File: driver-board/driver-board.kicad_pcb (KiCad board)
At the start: 2 copper layers, 105.1 x 41 mm, 78 parts, among them J1 Conn_01x02, J11 Conn_01x04, J2 Conn_01x02, J3 Conn_01x02, J4 Conn_01x02, J5 Conn_01x02, J6 Conn_01x02, J7 Conn_01x02, J8 Conn_01x02, J9 Conn_01x06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

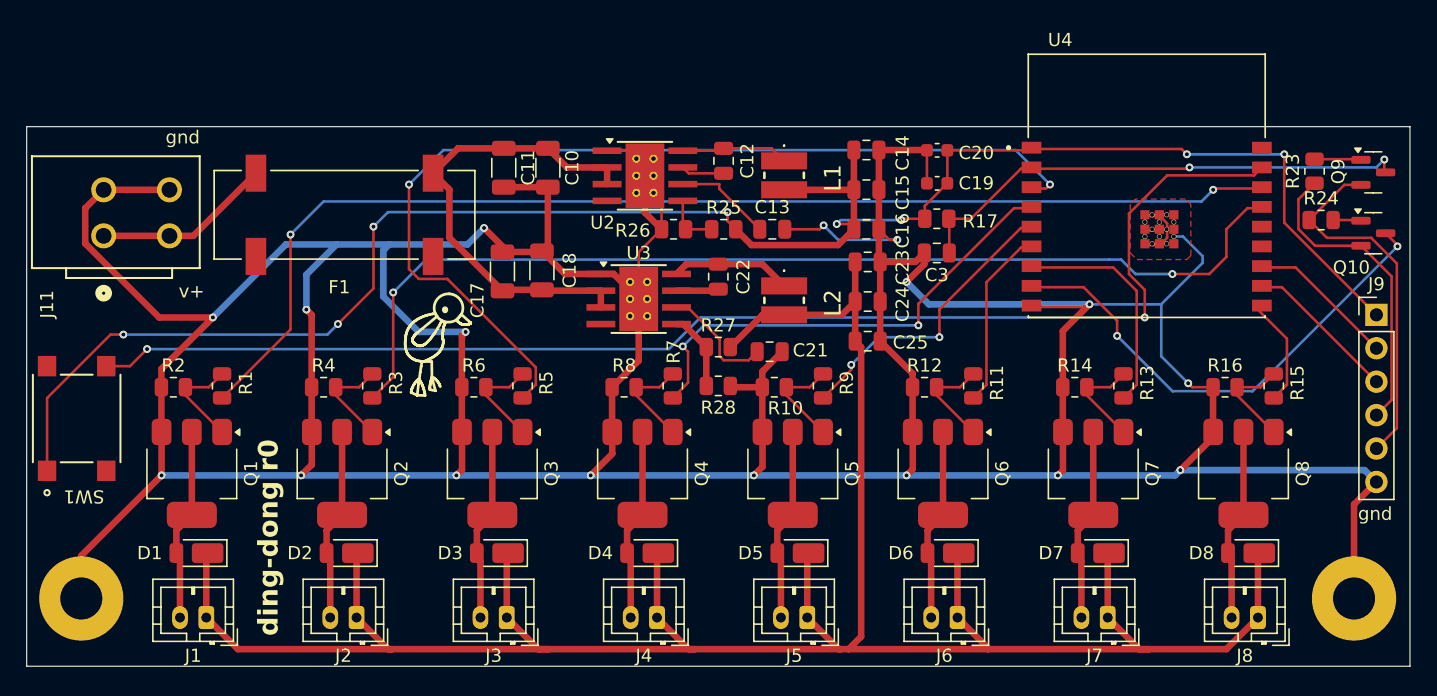
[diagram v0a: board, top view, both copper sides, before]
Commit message: updated layout
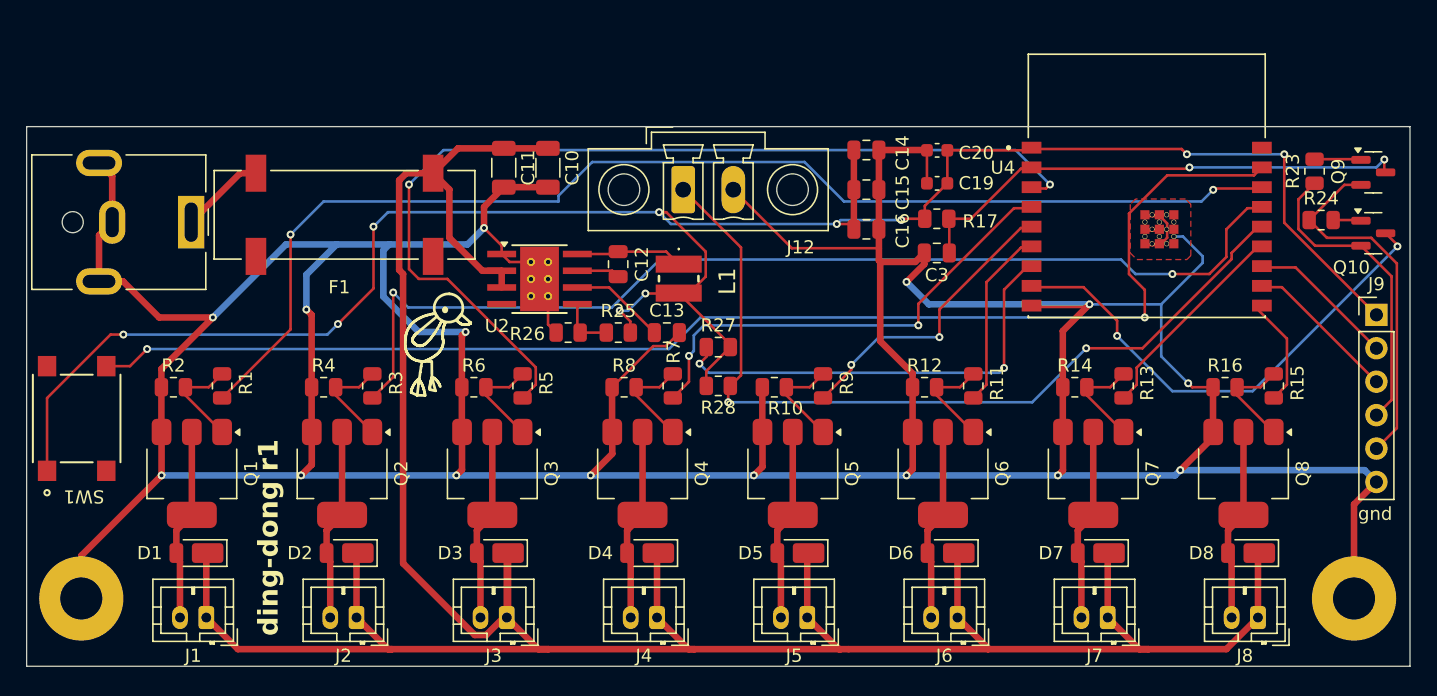
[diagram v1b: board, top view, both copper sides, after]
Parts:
- removed C17: 10uF 50V, Capacitor_SMD:C_1206_3216Metric
- removed C18: .022uF 50V, Capacitor_SMD:C_1206_3216Metric
- removed C21: 1uF, Capacitor_SMD:C_0805_2012Metric
- removed C22: 0.1uF, Capacitor_SMD:C_0805_2012Metric
- removed C23, C24, C25: 10uF, Capacitor_SMD:C_0805_2012Metric
- removed J11: Conn_01x04, footprints:CONN2_2601-3102_WAG
- removed L2: 47uH, footprints:SRN3010C2R2M
- removed U3: LMR36510ADDA, Package_SO:Texas_HTSOP-8-1EP_3.9x4.9mm_P1.27mm_EP2.95x4.9mm_Mask2.4x3.1mm_ThermalVias
- added J10: PJ-063AH, Connector_BarrelJack:BarrelJack_CUI_PJ-063AH_Horizontal, F.Cu at (75.8, 88.8)
- added J12: Conn_01x02, Connector_Phoenix_MC:PhoenixContact_MCV_1,5_2-GF-3.81_1x02_P3.81mm_Vertical_ThreadedFlange_MountHole, F.Cu at (113.1, 86.3)
- R27: value 100k -> 10k
- R28: value 9.09k -> 10k
- moved C12 11.2 mm to (108.2, 92.0)
- moved C13 11.2 mm to (111.9, 97.2)
- moved R25 11.2 mm to (108.2, 97.2)
- moved R26 11.2 mm to (104.4, 97.2)
- moved L1 11.2 mm to (112.8, 93.0)
- moved U2 11.2 mm to (102.2, 93.1)
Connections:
- C10 pad 1: /power/V_FUSED -> +12V
- C11 pad 1: /power/V_FUSED -> +12V
- F1 pad 2_1: /power/V_FUSED -> +12V
- R27 pad 1: Net-(U3-FB) -> Net-(U4-IO8)
- R27 pad 2: +12V -> +3.3V
- R28 pad 1: GND -> Net-(J12-Pin_1)
- R28 pad 2: Net-(U3-FB) -> +3.3V
- U2 pad 2: /power/V_FUSED -> +12V
- U2 pad 3: /power/V_FUSED -> +12V
- U4 pad 13: unconnected-(U4-IO18-Pad13) -> /c6
- U4 pad 14: unconnected-(U4-IO19-Pad14) -> Net-(J12-Pin_1)
- U4 pad 7: /c6 -> Net-(U4-IO8)
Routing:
- net Net-(J12-Pin_1): track 0.00 -> 64.9 mm, vias 0 -> 2
- net /power/V_FUSED: track 35.8 -> 0.00 mm
- net Net-(U4-IO8): track 0.00 -> 33.8 mm, vias 0 -> 2
- net GND: track 399.6 -> 369.4 mm, vias 17 -> 15
- net +12V: track 187.9 -> 215.7 mm
- net +3.3V: track 143.8 -> 161.4 mm, vias 8 -> 10
- net Net-(U3-SW): track 9.17 -> 0.00 mm
- net Net-(U3-VCC): track 8.81 -> 0.00 mm
- net Net-(F1-Pad1_1): track 13.5 -> 6.46 mm
- net Net-(U3-FB): track 5.94 -> 0.00 mm
- net Net-(U3-BOOT): track 3.22 -> 0.00 mm
- net /c0: track 89.3 -> 92.0 mm
- net /c6: track 17.8 -> 16.0 mm
- net /c1: track 79.0 -> 79.9 mm
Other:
- board text added: "ding-dong r1"
- board text removed: "ding-dong r0"
- board text removed: "v+"

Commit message: new board
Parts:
- removed Q1, Q2, Q3, Q4, Q5, Q6, Q7, Q8: BUK7880-55A, Package_TO_SOT_SMD:SOT-223-3_TabPin2
- added Q11: ZXM61N03FTA, Package_TO_SOT_SMD:SOT-23-3, F.Cu at (75.8, 108.8)
- added Q12: ZXM61N03FTA, Package_TO_SOT_SMD:SOT-23-3, F.Cu at (87.3, 108.8)
- added Q13: ZXM61N03FTA, Package_TO_SOT_SMD:SOT-23-3, F.Cu at (98.7, 108.8)
- added Q14: ZXM61N03FTA, Package_TO_SOT_SMD:SOT-23-3, F.Cu at (110.1, 108.8)
- added Q15: ZXM61N03FTA, Package_TO_SOT_SMD:SOT-23-3, F.Cu at (121.6, 108.8)
- added Q16: ZXM61N03FTA, Package_TO_SOT_SMD:SOT-23-3, F.Cu at (133.0, 108.8)
- added Q17: ZXM61N03FTA, Package_TO_SOT_SMD:SOT-23-3, F.Cu at (144.5, 108.8)
- added Q18: ZXM61N03FTA, Package_TO_SOT_SMD:SOT-23-3, F.Cu at (155.9, 108.8)
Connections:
- F1 pad 1_2: (no net) -> Net-(F1-Pad1_1)
- F1 pad 2_2: (no net) -> +12V
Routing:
- net GND: track 369.4 -> 384.7 mm
- net Net-(F1-Pad1_1): track 6.46 -> 12.5 mm
- net Net-(D1-A): track 14.7 -> 9.52 mm
- net Net-(D2-A): track 14.7 -> 9.53 mm
- net Net-(D3-A): track 14.7 -> 9.54 mm
- net Net-(D4-A): track 14.7 -> 9.56 mm
- net Net-(D5-A): track 14.7 -> 9.57 mm
- net Net-(D6-A): track 14.7 -> 9.58 mm
- net Net-(D7-A): track 14.7 -> 9.60 mm
- net Net-(D8-A): track 14.7 -> 9.61 mm
- net Net-(Q11-G): track 7.76 -> 10.7 mm
- net Net-(Q18-G): track 7.76 -> 10.2 mm
- net Net-(Q17-G): track 7.76 -> 10.2 mm
- net Net-(Q16-G): track 7.76 -> 10.2 mm
- net Net-(Q15-G): track 7.76 -> 10.2 mm
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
